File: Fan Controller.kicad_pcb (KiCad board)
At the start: 4 copper layers, 33 x 96 mm, 48 parts, among them J1 Power Input, J2 4-Pin Fan Header, J3 4-Pin Fan Header, J4 I2C, J5 I2C, J6 Expansion 1, J7 Expansion 2, Q1 SQD19P06-60L_GE3, U1 ESP32-C3-SuperMini, U2 AP63205QWU-7, U3 SN74LVC2G06DBVR, U4 AP63201QWU-7

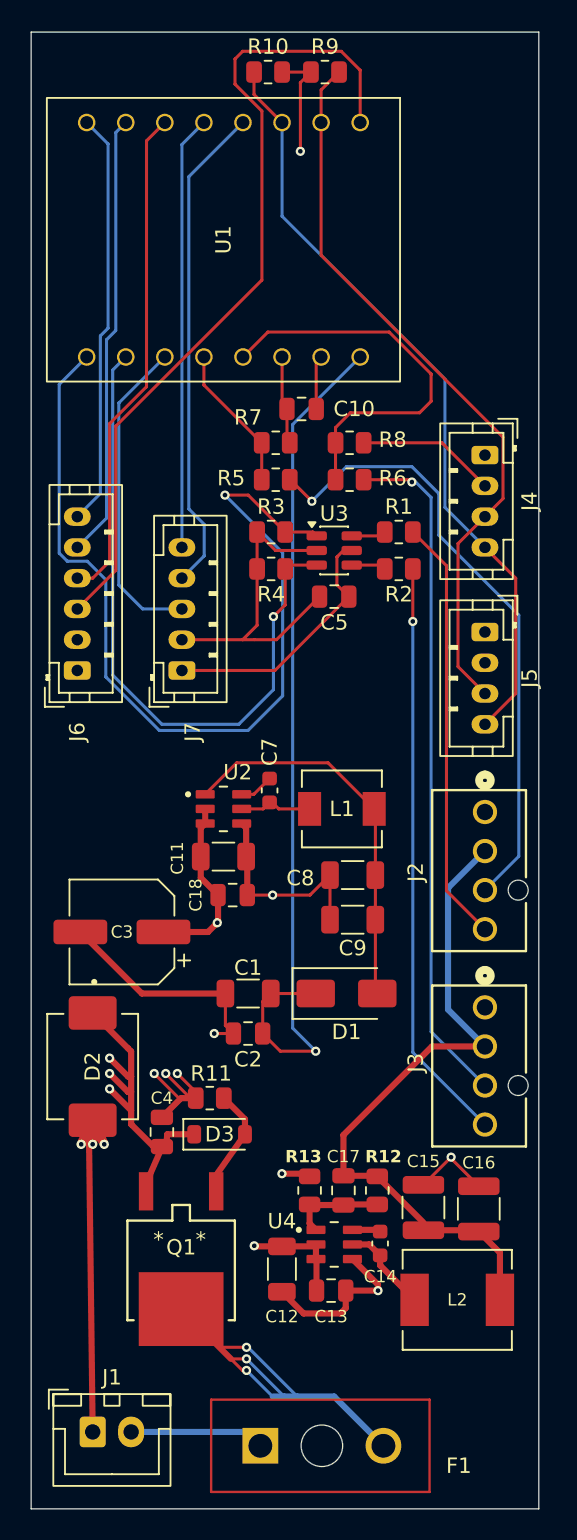
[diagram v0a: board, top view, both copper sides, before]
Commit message: Improvements around U2 placements
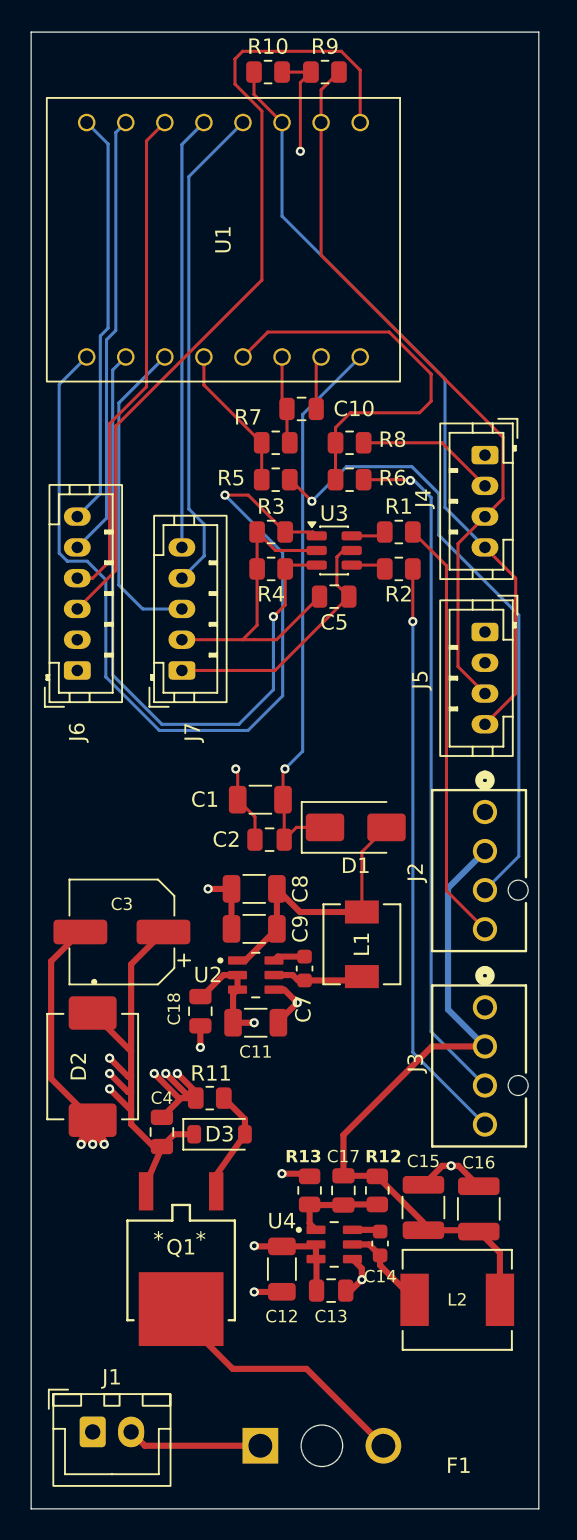
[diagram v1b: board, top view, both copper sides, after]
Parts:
- moved C2 12.7 mm to (167.0, 90.0)
- moved C1 12.6 mm to (166.4, 87.4)
- moved C7 11.8 mm to (169.3, 98.4)
- moved C11 11.0 mm to (166.1, 101.9)
- moved U2 11.0 mm to (166.1, 98.8)
- moved D1 10.8 mm to (172.6, 89.2)
- moved L1 8.90 mm to (173.0, 96.8), turned to 90 degrees
- moved C18 7.84 mm to (162.5, 101.2), turned to -90 degrees
- moved C8 6.46 mm to (166.0, 93.2)
- moved C9 6.43 mm to (166.0, 95.8)
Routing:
- net GND: track 107.5 -> 80.2 mm, vias 11 -> 14
- net /+5V_SYS: track 57.2 -> 37.6 mm
- net /12V_RAW_FUSED: track 35.7 -> 17.1 mm, vias 3 -> 0
- net /+5V_BUCK: track 25.2 -> 18.3 mm
- net /+12V_PROTECTED: track 41.2 -> 45.5 mm
- net Net-(U2-SW): track 5.16 -> 5.96 mm

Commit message: Corrections in routing, optimizations
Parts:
- moved R11 6.39 mm to (166.0, 112.5), turned to 90 degrees
- moved C3 4.52 mm to (157.0, 91.5), turned to -90 degrees
- moved D2 1.25 mm to (155.5, 106.0), turned to 90 degrees
- moved C12 1.09 mm to (167.8, 119.0)
- moved F1 0.90 mm to (170.4, 128.5)
- moved D3 0.43 mm to (163.5, 109.5)
- moved C18 0.15 mm to (162.5, 101.0)
- moved C11 0.10 mm to (166.0, 101.9)
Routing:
- net GND: track 80.2 -> 58.8 mm, vias 14 -> 15
- net /+12V_PROTECTED: track 45.5 -> 31.3 mm, vias 5 -> 6
- net /+12V_FAN: track 45.0 -> 46.4 mm
- net Net-(D3-A): track 6.39 -> 5.44 mm

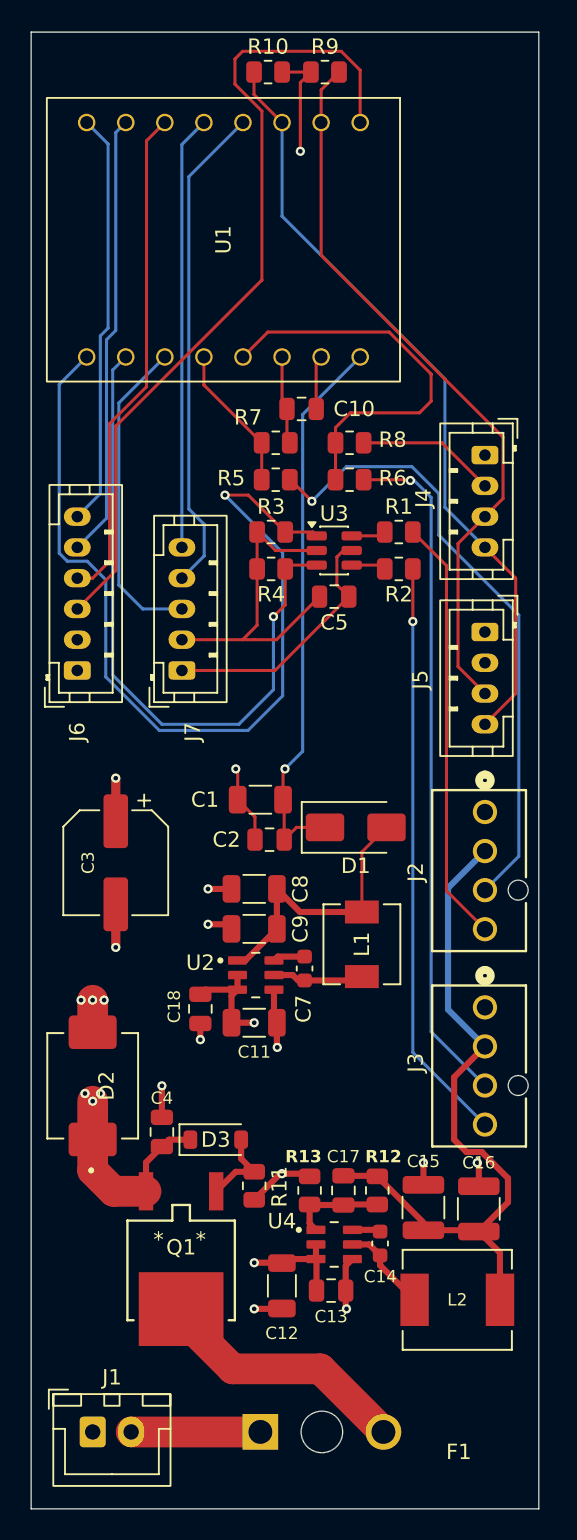
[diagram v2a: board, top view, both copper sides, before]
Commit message: Better buck power reliability. Better placement of some distant elements.
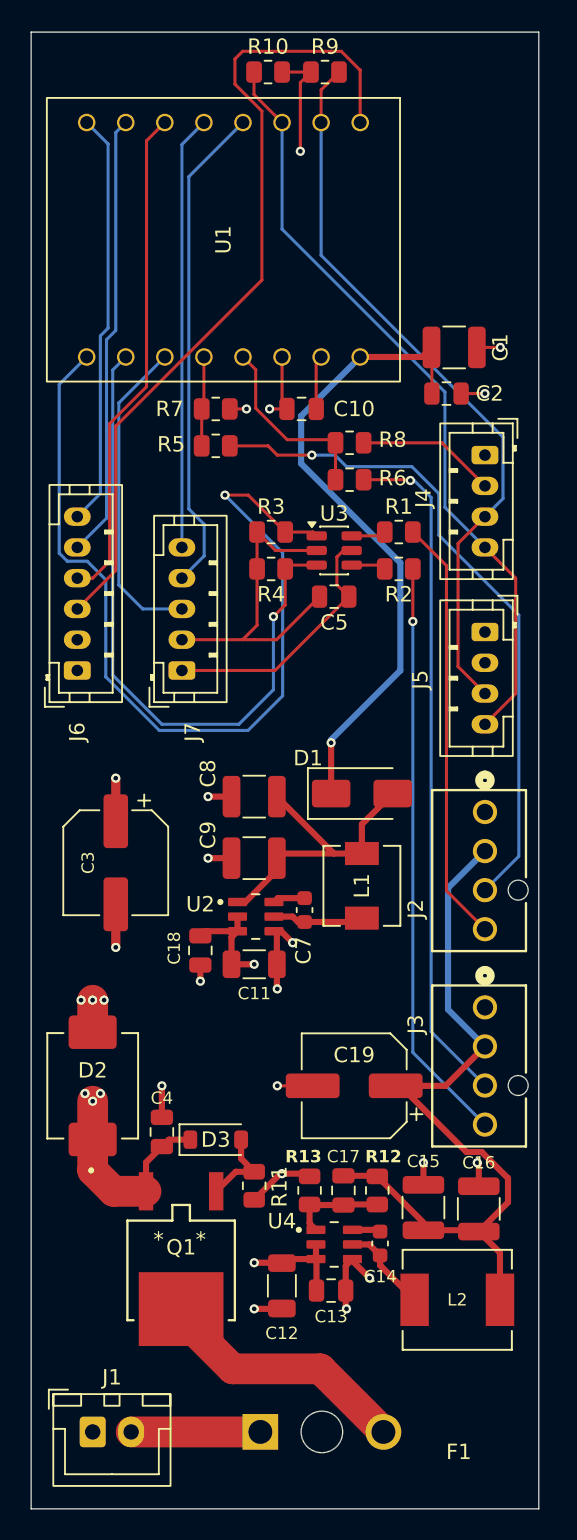
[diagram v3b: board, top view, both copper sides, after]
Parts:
- added C19: 47µF / 25V Hybrid, Capacitor_SMD:CP_Elec_6.3x5.8, F.Cu at (172.5, 106.0)
- C1: value 10µF -> 47µF; footprint Capacitor_SMD:C_1206_3216Metric -> Capacitor_SMD:C_1210_3225Metric
- C8, C9: value 22µF -> 47µF; footprint Capacitor_SMD:C_1206_3216Metric -> Capacitor_SMD:C_1210_3225Metric
- R1, R2: value 100R -> 47R
- moved C1 32.0 mm to (179.0, 58.0), turned to 0 degrees
- moved C2 31.2 mm to (178.5, 61.0), turned to 0 degrees
- moved C8 6.00 mm to (166.0, 87.2)
- moved C9 4.60 mm to (166.0, 91.2)
- moved R7 4.48 mm to (163.5, 62.0)
- moved R5 4.48 mm to (163.5, 64.4)
- moved C11 3.80 mm to (166.0, 98.1)
- moved C18 3.80 mm to (162.5, 97.2)
- moved C7 3.80 mm to (169.3, 94.6)
- moved L1 3.80 mm to (173.0, 93.0)
- moved U2 3.80 mm to (166.1, 95.0)
- moved D1 2.24 mm to (173.0, 87.0)
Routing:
- net /FAN2_TACH_GPIO: track 26.1 -> 12.2 mm
- net /+12V_FAN: track 46.4 -> 51.6 mm
- net /+5V_SYS: track 37.6 -> 42.4 mm
- net /FAN1_TACH_GPIO: track 9.54 -> 5.84 mm
- net GND: track 58.8 -> 62.5 mm, vias 15 -> 19
- net /+5V_BUCK: track 18.3 -> 21.6 mm
- net Net-(J2-Pin_3): track 40.8 -> 43.7 mm
- net /+3V3: track 39.2 -> 39.1 mm, vias 1 -> 3

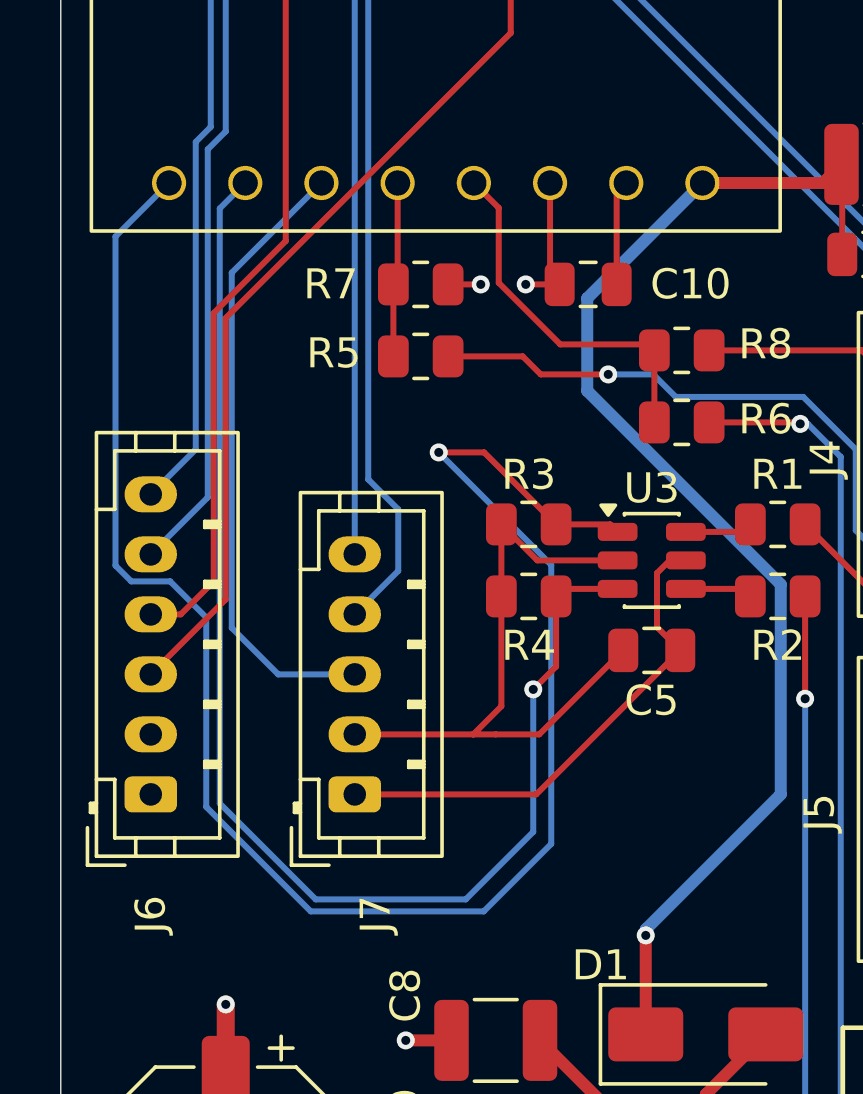
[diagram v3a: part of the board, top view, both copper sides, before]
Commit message: R1 and 2 were 47k items added to manufacturing instead of 47R
some placement optimizations
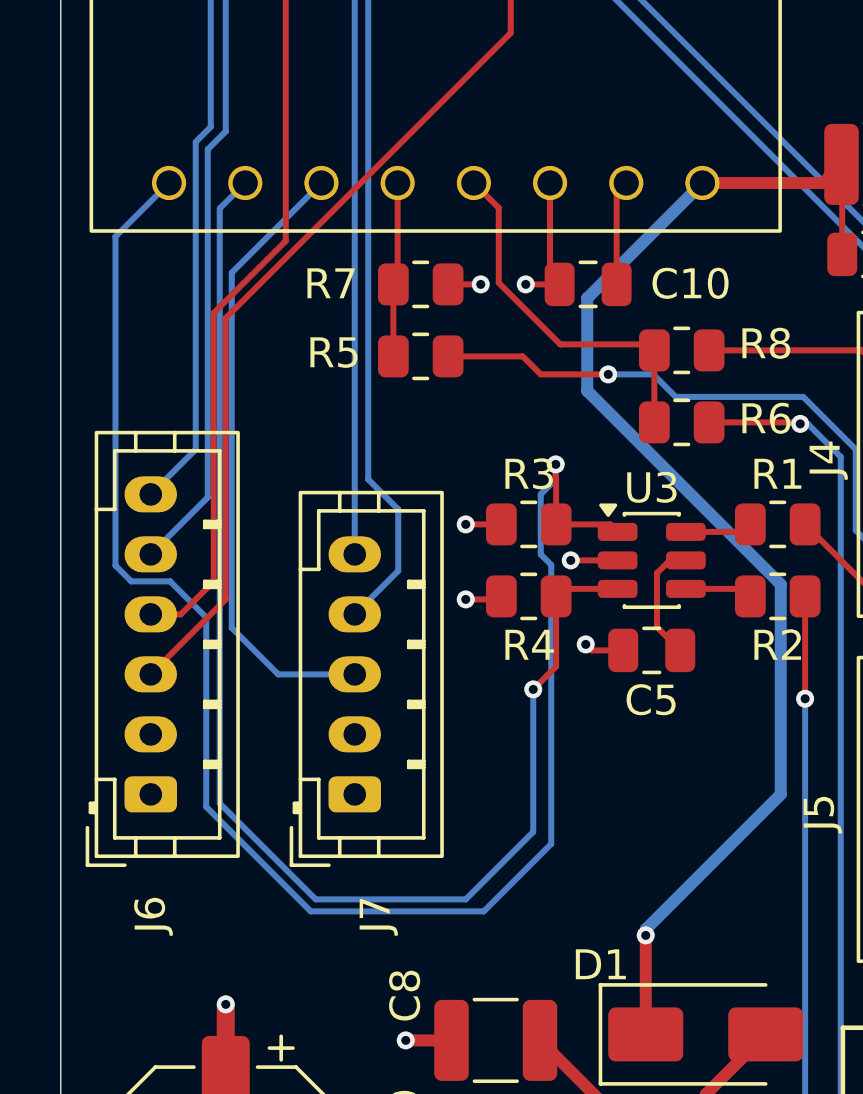
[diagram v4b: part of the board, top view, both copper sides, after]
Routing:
- net GND: track 62.5 -> 45.9 mm, vias 19 -> 23
- net /+3V3: track 39.1 -> 26.3 mm
- net /FAN1_PWM_GPIO: track 59.1 -> 54.6 mm

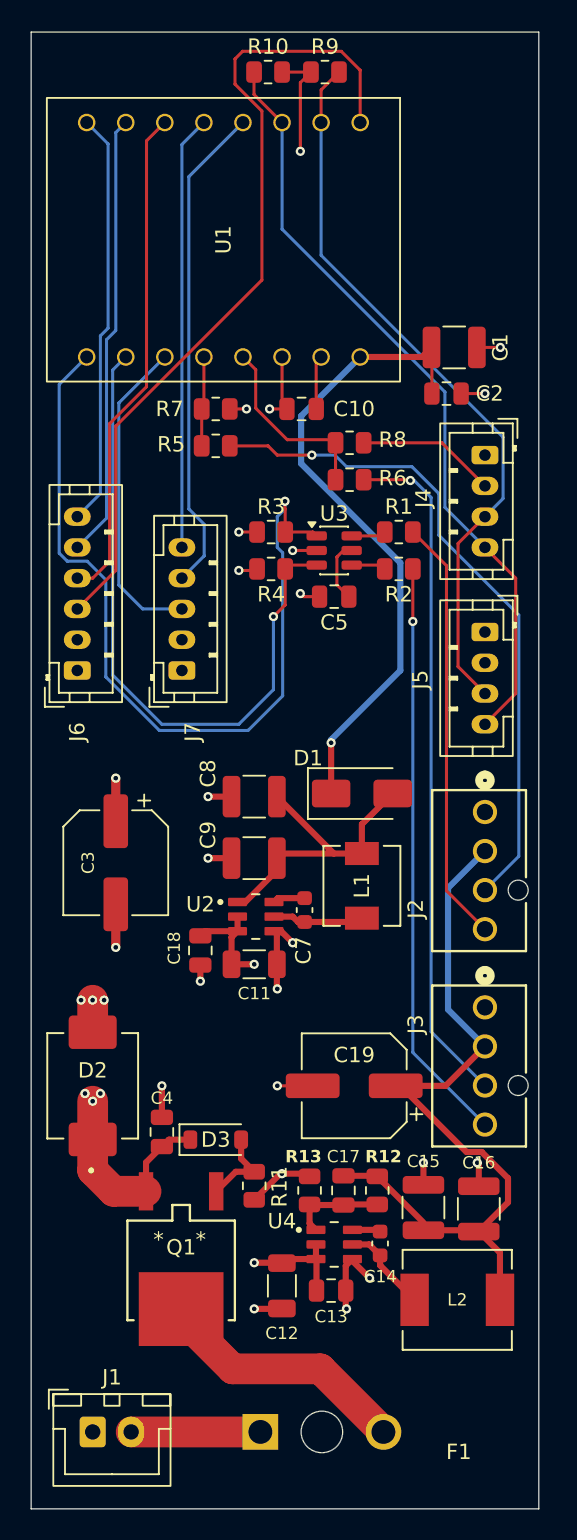
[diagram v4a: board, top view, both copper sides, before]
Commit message: Redesigned the 3V3 layout resulting in a much neater trace run. Widened the power rails
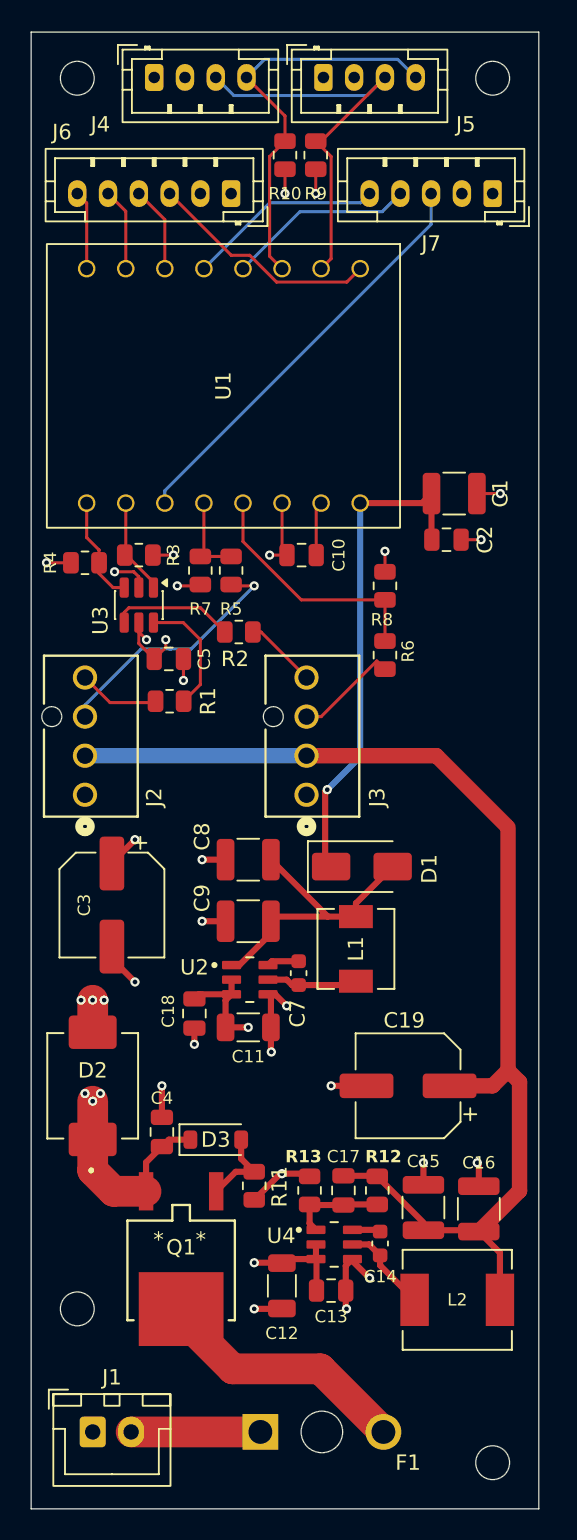
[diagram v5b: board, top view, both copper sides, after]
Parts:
- added H1: MountingHole_2.2mm_M2, MountingHole:MountingHole_2.2mm_M2, F.Cu at (154.5, 40.5)
- added H2: MountingHole_2.2mm_M2, MountingHole:MountingHole_2.2mm_M2, F.Cu at (181.5, 40.5)
- added H3: MountingHole_2.2mm_M2, MountingHole:MountingHole_2.2mm_M2, F.Cu at (154.5, 120.5)
- added H4: MountingHole_2.2mm_M2, MountingHole:MountingHole_2.2mm_M2, F.Cu at (181.5, 130.5)
- moved J5 37.5 mm to (170.5, 40.5), turned to 0 degrees
- moved J7 37.0 mm to (181.5, 48.0), turned to 180 degrees
- moved J4 32.6 mm to (159.5, 40.5), turned to 0 degrees
- moved J6 32.6 mm to (164.5, 48.0), turned to 180 degrees
- moved J2 26.0 mm to (155.0, 87.1), turned to -90 degrees
- moved R1 18.5 mm to (160.5, 81.0), turned to 180 degrees
- moved J3 18.0 mm to (169.4, 87.1), turned to -90 degrees
- moved U3 13.2 mm to (158.5, 74.8), turned to -90 degrees
- moved R4 12.1 mm to (155.0, 72.0)
- moved R6 11.6 mm to (174.5, 78.0), turned to 90 degrees
- moved C5 11.5 mm to (160.4, 78.2), turned to 0 degrees
- moved R2 11.2 mm to (165.0, 76.5)
- moved R7 10.5 mm to (162.5, 72.5), turned to -90 degrees
- moved R8 9.58 mm to (174.5, 73.5), turned to 90 degrees
- moved C1 9.50 mm to (179.0, 67.5)
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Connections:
- U1 pad 0: /FAN1_PWM_GPIO -> /FAN2_PWM_GPIO
- U1 pad 1: /FAN2_PWM_GPIO -> /FAN1_PWM_GPIO
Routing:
- net /FAN1_PWM_GPIO: track 54.6 -> 6.44 mm, vias 1 -> 0
- net /GPIO5: track 53.7 -> 15.1 mm
- net Net-(J3-Pin_3): track 44.5 -> 6.82 mm, vias 1 -> 0
- net /FAN2_PWM_GPIO: track 44.1 -> 7.16 mm, vias 1 -> 0
- net /FAN2_PWM: track 38.1 -> 4.71 mm, vias 1 -> 0
- net Net-(J2-Pin_3): track 43.7 -> 16.5 mm
- net /GPIO10: track 32.6 -> 5.58 mm
- net /+12V_FAN: track 51.6 -> 77.2 mm
- net /I2C_SCL: track 50.3 -> 26.3 mm
- net /GPIO20: track 28.9 -> 5.36 mm
- net /FAN1_PWM: track 27.8 -> 5.17 mm
- net /GPIO21: track 27.0 -> 5.13 mm
- net /I2C_SDA: track 47.7 -> 27.2 mm
- net /GPIO8: track 32.1 -> 12.3 mm
- net /GPIO9: track 28.2 -> 12.8 mm
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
